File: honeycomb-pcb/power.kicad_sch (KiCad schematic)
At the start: 6 parts, among them Q301 MOSFET-P-CH-EN_60V_50A, Q302 MOSFET-N-CH-EN_100V_260mA, T301 TERM_BLK_HDR_2POS_90DEG_0.2IN

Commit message: tmc5130-uart-multiplexer -> honeycomb-pcb
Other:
- title: tmc5130-uart-multiplexer -> honeycomb-pcb
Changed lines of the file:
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@@
   (paper "A4")
   (title_block
-    (title "tmc5130-uart-multiplexer")
+    (title "honeycomb-pcb")
     (date "2024-07-10")
     (rev "1.0")
@@
     (pin "1")
     (instances
-      (project "tmc5130-uart-multiplexer"
+      (project "honeycomb-pcb"
         (path "/df2b2e89-e055-4140-95de-f1df723db034/c1dd8f61-494c-402f-8e59-08309c64fc3f"
           (reference "T301") (unit 1)
@@
     (pin "1")
     (instances
-      (project "tmc5130-uart-multiplexer"
+      (project "honeycomb-pcb"
         (path "/df2b2e89-e055-4140-95de-f1df723db034/c1dd8f61-494c-402f-8e59-08309c64fc3f"
           (reference "#FLG0301") (unit 1)
@@
     (pin "1")
     (instances
-      (project "tmc5130-uart-multiplexer"
+      (project "honeycomb-pcb"
         (path "/df2b2e89-e055-4140-95de-f1df723db034/c1dd8f61-494c-402f-8e59-08309c64fc3f"
           (reference "Q301") (unit 1)
@@
     (pin "1")
     (instances
-      (project "tmc5130-uart-multiplexer"
+      (project "honeycomb-pcb"
         (path "/df2b2e89-e055-4140-95de-f1df723db034/c1dd8f61-494c-402f-8e59-08309c64fc3f"
           (reference "#FLG0302") (unit 1)
@@
     (pin "1")
     (instances
-      (project "tmc5130-uart-multiplexer"
+      (project "honeycomb-pcb"
         (path "/df2b2e89-e055-4140-95de-f1df723db034/c1dd8f61-494c-402f-8e59-08309c64fc3f"
           (reference "R301") (unit 1)
@@
     (pin "2")
     (instances
-      (project "tmc5130-uart-multiplexer"
+      (project "honeycomb-pcb"
         (path "/df2b2e89-e055-4140-95de-f1df723db034/c1dd8f61-494c-402f-8e59-08309c64fc3f"
           (reference "D301") (unit 1)
@@
     (pin "2")
     (instances
-      (project "tmc5130-uart-multiplexer"
+      (project "honeycomb-pcb"
         (path "/df2b2e89-e055-4140-95de-f1df723db034/c1dd8f61-494c-402f-8e59-08309c64fc3f"
           (reference "R302") (unit 1)
@@
     (pin "1")
     (instances
-      (project "tmc5130-uart-multiplexer"
+      (project "honeycomb-pcb"
         (path "/df2b2e89-e055-4140-95de-f1df723db034/c1dd8f61-494c-402f-8e59-08309c64fc3f"
           (reference "#FLG0303") (unit 1)
@@
     (pin "2")
     (instances
-      (project "tmc5130-uart-multiplexer"
+      (project "honeycomb-pcb"
         (path "/df2b2e89-e055-4140-95de-f1df723db034/c1dd8f61-494c-402f-8e59-08309c64fc3f"
           (reference "Q302") (unit 1)

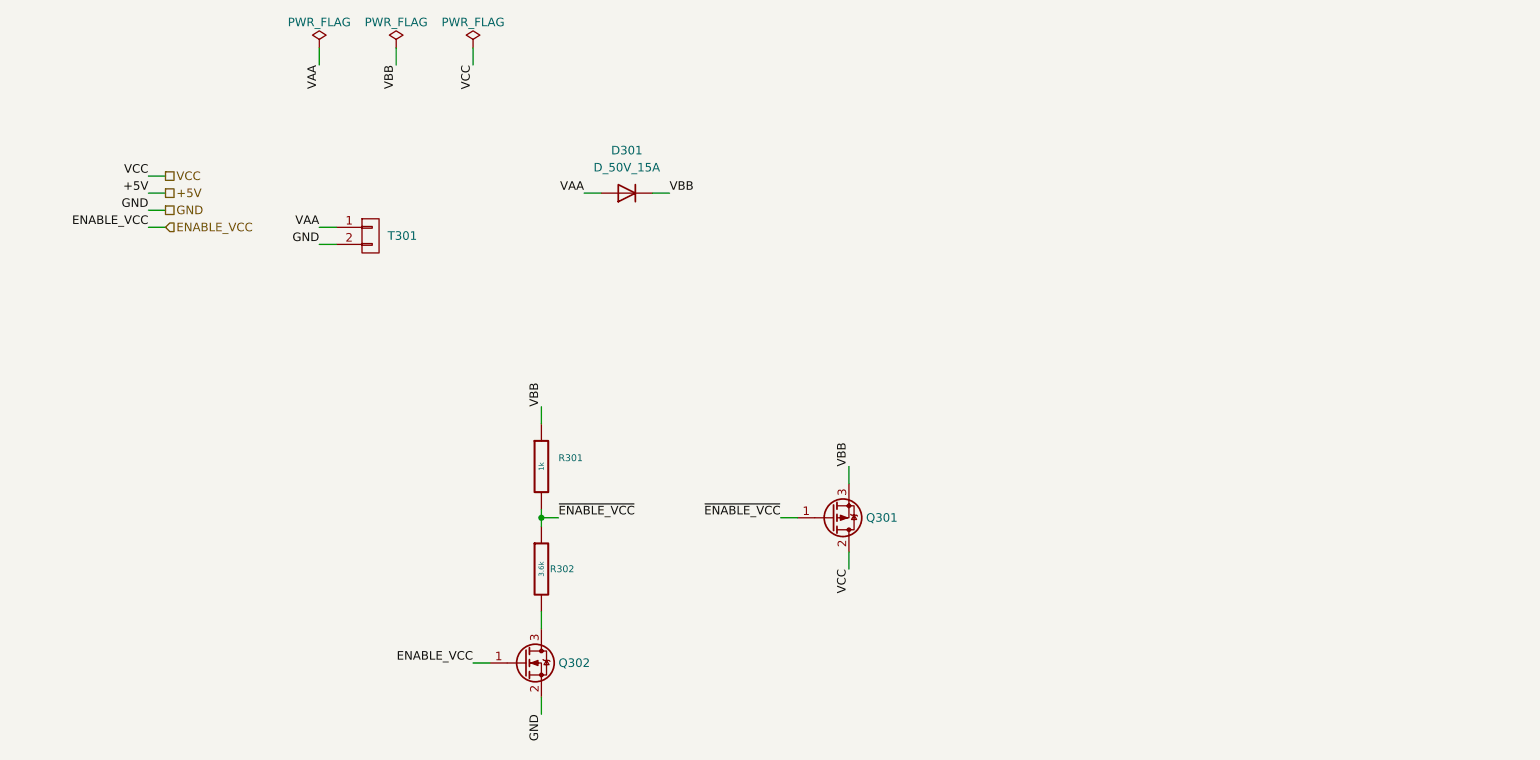
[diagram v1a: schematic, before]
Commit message: motor -> prism
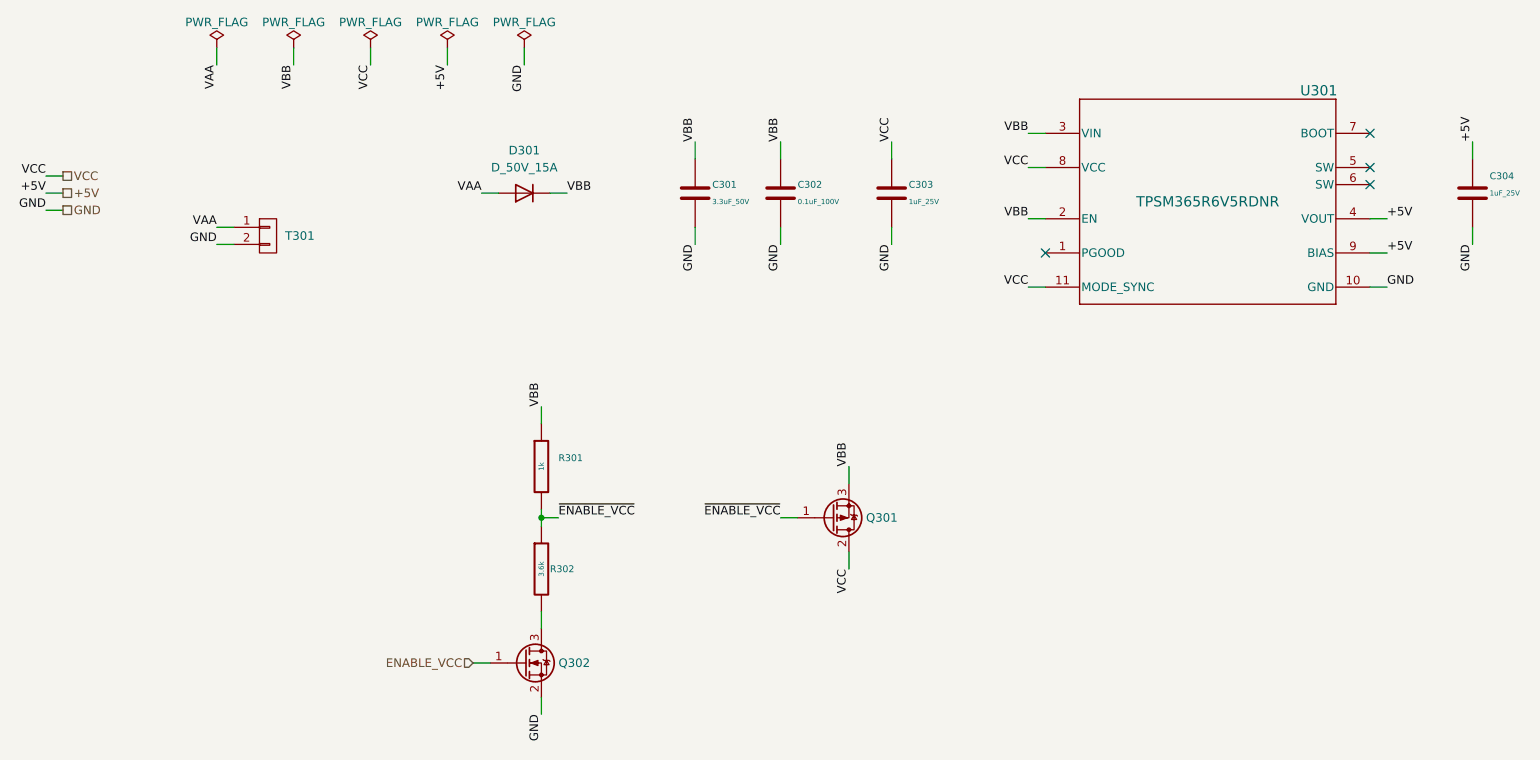
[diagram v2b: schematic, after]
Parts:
- added C301: 3.3uF_50V, Janelia:C_1210_3225Metric, symbol Janelia:C_3.3uF_50V_1210
- added C302: 0.1uF_100V, Janelia:C_0402_1005Metric, symbol Janelia:C_0.1uF_100V_0402
- added C303, C304: 1uF_25V, Janelia:C_0402_1005Metric, symbol Janelia:C_1uF_25V_0402
- added U301: TPSM365R6V5RDNR, Janelia:RDN0011A-MFG, symbol Janelia:TPSM365R6V5RDNR
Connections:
- net +5V: now also C304.1, U301.4 (VOUT), U301.9 (BIAS)
- net GND: now also C301.2, C302.2, C303.2, C304.2, U301.10 (GND)
- net VBB: now also C301.1, C302.1, U301.2 (EN), U301.3 (VIN)
- net VCC: now also C303.1, U301.11 (MODE_SYNC), U301.8 (VCC)
- no-connect marks 0 -> 4
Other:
- moved on the sheet: D301, T301

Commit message: Update BOM
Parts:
- added M301: Fan_5VDC_25x25x8mm, Janelia:FAN_5VDC_25x25x8mm, symbol Janelia:Fan_5VDC_25x25x8mm
- U301: Package (none) -> QFN-11(3.5x4.5); Synopsis 3-V TO 65-V INPUT, 1-V TO 13-V O -> DC-DC 5V 600mA Output 3-65V Input
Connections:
- net +5V: now also M301.1 (+5V)
- net GND: now also M301.2 (GND), M301.3 (MH)
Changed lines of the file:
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@@
   (title_block
     (title "honeycomb-pcb")
-    (date "2024-07-12")
+    (date "2024-07-16")
     (rev "1.0")
     (company "Howard Hughes Medical Institute")
@@
     (stroke (width 0) (type default))
   )
+  (wire (pts (xy 208.28 127) (xy 208.28 129.54))
+    (stroke (width 0) (type default))
+  )
   (wire (pts (xy 167.64 66.04) (xy 167.64 68.58))
     (stroke (width 0) (type default))
@@
     (stroke (width 0) (type default))
   )
+  (wire (pts (xy 208.28 109.22) (xy 208.28 106.68))
+    (stroke (width 0) (type default))
+  )
   (wire (pts (xy 153.67 109.22) (xy 151.13 109.22))
     (stroke (width 0) (type default))
@@
     (effects (font (size 1.27 1.27)) (justify right bottom))
   )
+  (label "+5V" (at 208.28 106.68 90) (fields_autoplaced)
+    (effects (font (size 1.27 1.27)) (justify left bottom))
+  )
   (label "GND" (at 167.64 68.58 270) (fields_autoplaced)
     (effects (font (size 1.27 1.27)) (justify right bottom))
@@
   (label "+5V" (at 241.3 64.77 0) (fields_autoplaced)
     (effects (font (size 1.27 1.27)) (justify left bottom))
+  )
+  (label "GND" (at 208.28 129.54 270) (fields_autoplaced)
+    (effects (font (size 1.27 1.27)) (justify right bottom))
   )
   (label "GND" (at 151.13 68.58 270) (fields_autoplaced)
@@
       (effects (font (size 1.27 1.27) italic) hide)
     )
-    (property "Synopsis" "3-V TO 65-V INPUT, 1-V TO 13-V O" (at 214.63 36.83 0)
+    (property "Synopsis" "DC-DC 5V 600mA Output 3-65V Input" (at 214.63 36.83 0)
       (effects (font (size 1.27 1.27)) hide)
     )
@@
     )
     (property "LCSC" "C19078014" (at 214.63 44.45 0)
+      (effects (font (size 1.27 1.27)) hide)
+    )
+    (property "Package" "QFN-11(3.5x4.5)" (at 214.63 62.23 0)
       (effects (font (size 1.27 1.27)) hide)
     )
@@
         )
       )
+    )
+  )
+  (symbol (lib_id "Janelia:Fan_5VDC_25x25x8mm") (at 208.28 118.11 0) (unit 1)
+    (in_bom no) (on_board yes) (dnp no) (fields_autoplaced)
+    (property "Reference" "M301" (at 212.09 118.11 0) (do_not_autoplace)
+      (effects (font (size 1.27 1.27)) (justify left))
+    )
+    (property "Value" "Fan_5VDC_25x25x8mm" (at 208.28 113.03 0) (do_not_autoplace)
+      (effects (font (size 1.27 1.27)) (justify top) hide)
+    )
+    (property "Footprint" "Janelia:FAN_5VDC_25x25x8mm" (at 208.28 100.33 0)
+      (effects (font (size 1.27 1.27)) hide)
+    )
+    (property "Datasheet" "~" (at 208.28 101.6 0)
+      (effects (font (size 1.27 1.27)) hide)
+    )
+    (property "Synopsis" "FAN AXIAL 25X8MM 5VDC WIRE" (at 208.28 111.76 0)
+      (effects (font (size 1.27 1.27)) hide)
+    )
+    (property "Manufacturer" "ebm-papst Inc." (at 208.28 109.22 0)
+      (effects (font (size 1.27 1.27)) hide)
+    )
+    (property "Manufacturer Part Number" "255M" (at 208.28 110.49 0) (do_not_autoplace)
+      (effects (font (size 1.27 1.27)) hide)
+    )
+    (property "Vendor" "Digi-Key" (at 208.28 106.68 0)
+      (effects (font (size 1.27 1.27)) hide)
+    )
+    (property "Vendor Part Number" "381-2353-ND" (at 208.28 104.14 0)
+      (effects (font (size 1.27 1.27)) hide)
+    )
+    (property "LCSC" "" (at 208.28 118.11 0)
+      (effects (font (size 1.27 1.27)) hide)
+    )
+    (property "Sim.Enable" "0" (at 208.28 118.11 0)
+      (effects (font (size 1.27 1.27)) hide)
+    )
+    (pin "2")
+    (pin "3")
+    (pin "1")
+    (instances
+      (project "honeycomb-pcb"
+        (path "/df2b2e89-e055-4140-95de-f1df723db034/c1dd8f61-494c-402f-8e59-08309c64fc3f"
+          (reference "M301") (unit 1)
+        )
+      )

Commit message: Last update before renaming
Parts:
- T301: LCSC (none) -> C90074; Package (none) -> Push-Pull P=5.08mm
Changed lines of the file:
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@@
+      (effects (font (size 1.27 1.27)) hide)
+    )
+    (property "LCSC" "C90074" (at 74.93 67.31 0)
+      (effects (font (size 1.27 1.27)) hide)
+    )
+    (property "Package" "Push-Pull P=5.08mm" (at 74.93 67.31 0)
       (effects (font (size 1.27 1.27)) hide)
     )
